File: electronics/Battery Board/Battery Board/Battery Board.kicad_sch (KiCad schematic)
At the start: 1 part

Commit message: Battery Protection Circuit
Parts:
- removed U?: MAX1924XEEE+, SOP63P602X175-16N, symbol MAX1924XEEE_:MAX1924XEEE+
- added BT1: BK-18650-PC8, BAT_BK-18650-PC8, symbol BK-18650-PC8:BK-18650-PC8
- added C1: 2.2uF, Capacitor_SMD:C_0805_2012Metric_Pad1.18x1.45mm_HandSolder, symbol Device:C_Small
- added C2, C4, C5, C6: 0.1uF, Capacitor_SMD:C_0805_2012Metric_Pad1.18x1.45mm_HandSolder, symbol Device:C_Small
- added C3: 1uF, Capacitor_SMD:C_0805_2012Metric_Pad1.18x1.45mm_HandSolder, symbol Device:C_Small
- added D1: D_Schottky, Bluesat:SOT91P240X102-3N, symbol Device:D_Schottky
- added Q1, Q2: IRF7404, Package_SO:SOIC-8_3.9x4.9mm_P1.27mm, symbol Transistor_FET:IRF7404
- added R1, R2, R3: 1K, Resistor_SMD:R_0603_1608Metric_Pad0.98x0.95mm_HandSolder, symbol Device:R
- added R4: 51, Resistor_SMD:R_0603_1608Metric_Pad0.98x0.95mm_HandSolder, symbol Device:R
- added R5, R6, R7: 10K, Resistor_SMD:R_0603_1608Metric_Pad0.98x0.95mm_HandSolder, symbol Device:R
- added R8: Rocket_Board, Bluesat:Rocket_Layout, symbol BlueSat:Rocket_Board
- added R_{SENSE}1: 0.02, Resistor_SMD:R_0603_1608Metric_Pad0.98x0.95mm_HandSolder, symbol Device:R
- added U1: MAX1924XEEE+, SOP63P602X175-16N, symbol MAX1924XEEE_:MAX1924XEEE+
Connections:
- new net: C2.1, D1.1 (K), U1.2 (VCC)
- new net: R1.1, U1.7 (B1P)
- new net: BT1.1+, BT1.2-, C5.1, C6.2, R1.2
- new net: R8.1 (5V), R8.18 (5V), R8.23 (5V), R8.33 (5V), R8.40 (5V), R8.8 (5V)
- new net: R8.10 (3.3V), R8.20 (3.3V), R8.21 (3.3V), R8.3 (3.3V), R8.31 (3.3V), R8.38 (3.3V)
- new net: R8.11 (GND), R8.14 (GND), R8.17 (GND), R8.19 (GND), R8.2 (GND), R8.22 (GND), R8.24 (GND), R8.27 (GND), R8.30 (GND), R8.32 (GND), R8.34 (GND), R8.37 (GND), R8.39 (GND), R8.4 (GND), R8.7 (GND), R8.9 (GND)
- new net: R3.1, U1.3 (B3P)
- new net: BT1.3+, BT1.4-, C3.1, C4.2, R3.2
- new net: R6.1, U1.12 (SHDN)
- new net: BT1.4+, C3.2, D1.2 (A), Q2.5 (D), Q2.6 (D), Q2.7 (D), Q2.8 (D), R4.2
- new net: R5.2, U1.11 (CTL)
- new net: C1.2, R7.1, U1.16 (SRC)
- new net: R4.1, U1.1 (B4P)
- new net: BT1.2+, BT1.3-, C4.1, C5.2, R2.2
- new net: Q1.1 (S), Q1.2 (S), Q1.3 (S), Q2.1 (S), Q2.2 (S), Q2.3 (S), R7.2
- new net: Q1.4 (G), U1.15 (~{DSO})
- new net: R2.1, U1.5 (B2P)
- new net: Q2.4 (G), U1.13 (~{TKO})
- new net GND: R_{SENSE}1.1, U1.10 (PKN)
- new net GNDPWR: BT1.1-, C1.1, C2.2, C6.1, R5.1, R6.2, R_{SENSE}1.2, U1.9 (BN)
- new net VPP: Q1.5 (D), Q1.6 (D), Q1.7 (D), Q1.8 (D)

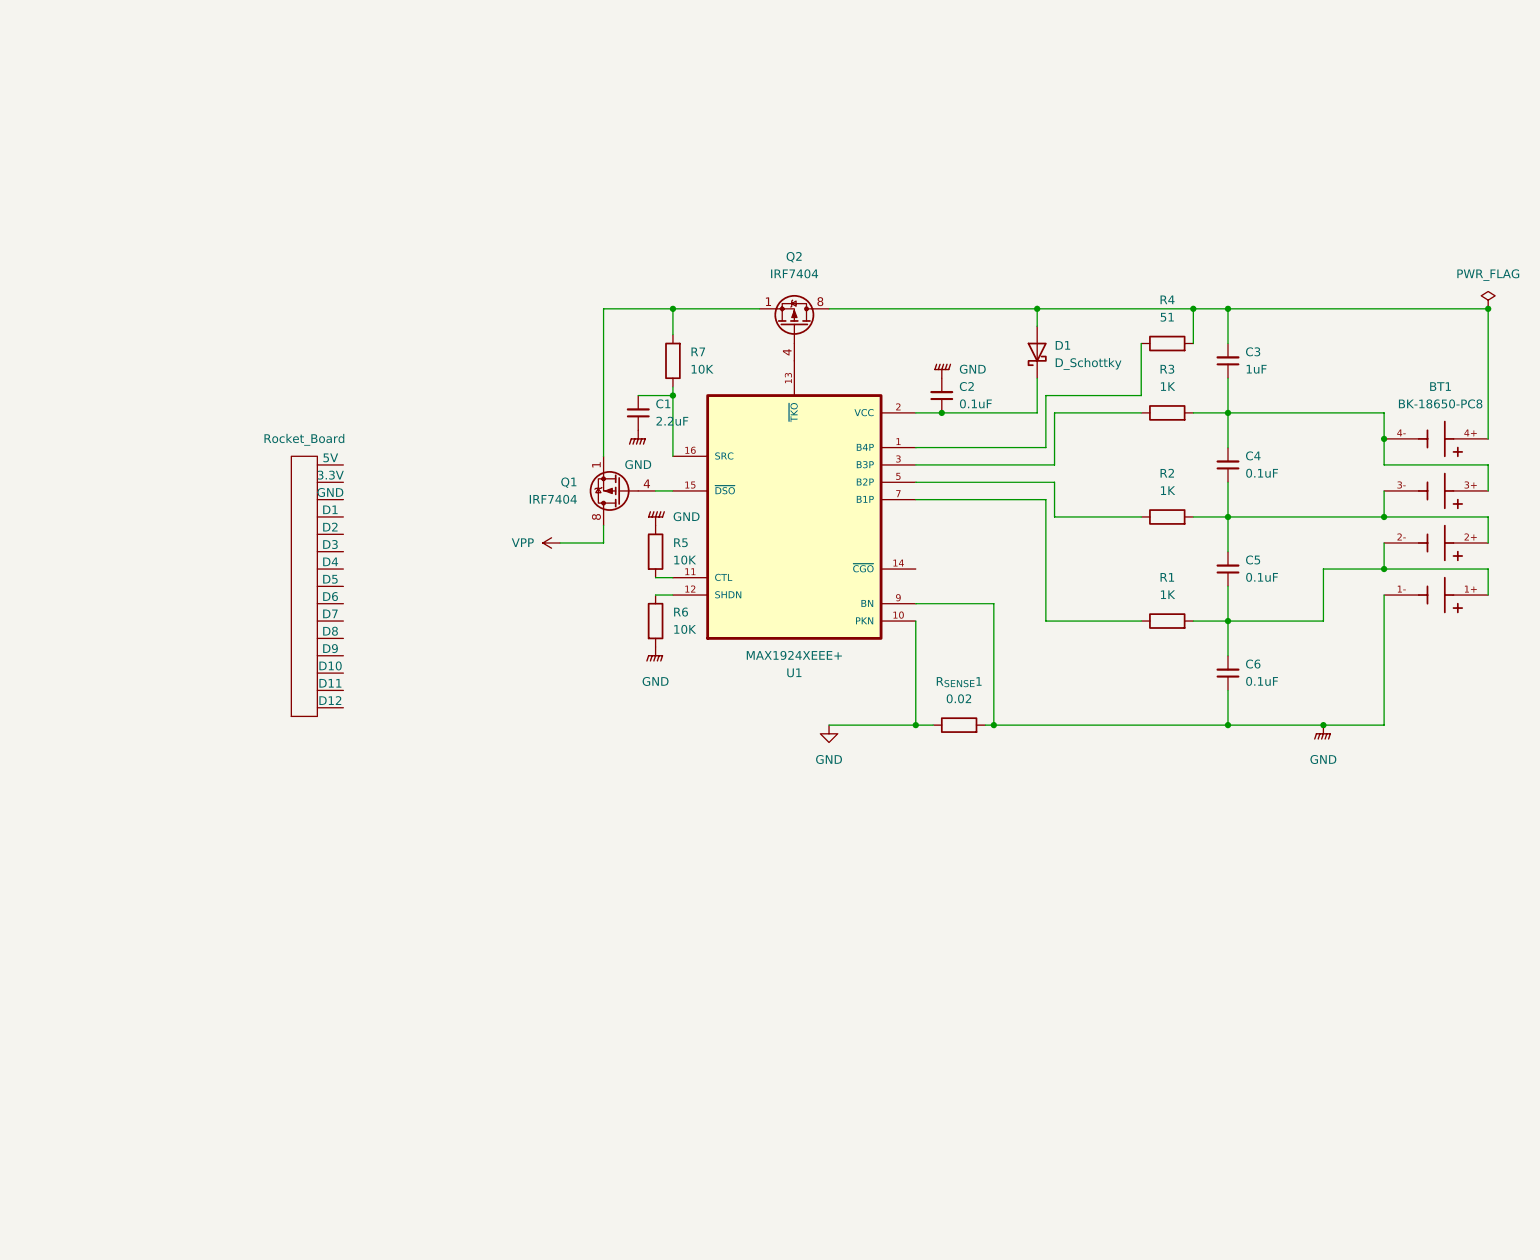
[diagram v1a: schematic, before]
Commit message: Batter Board almost finished
TODO
- Change mosfets&shunt resistor to new choice
- Adjust inductor for higher voltage
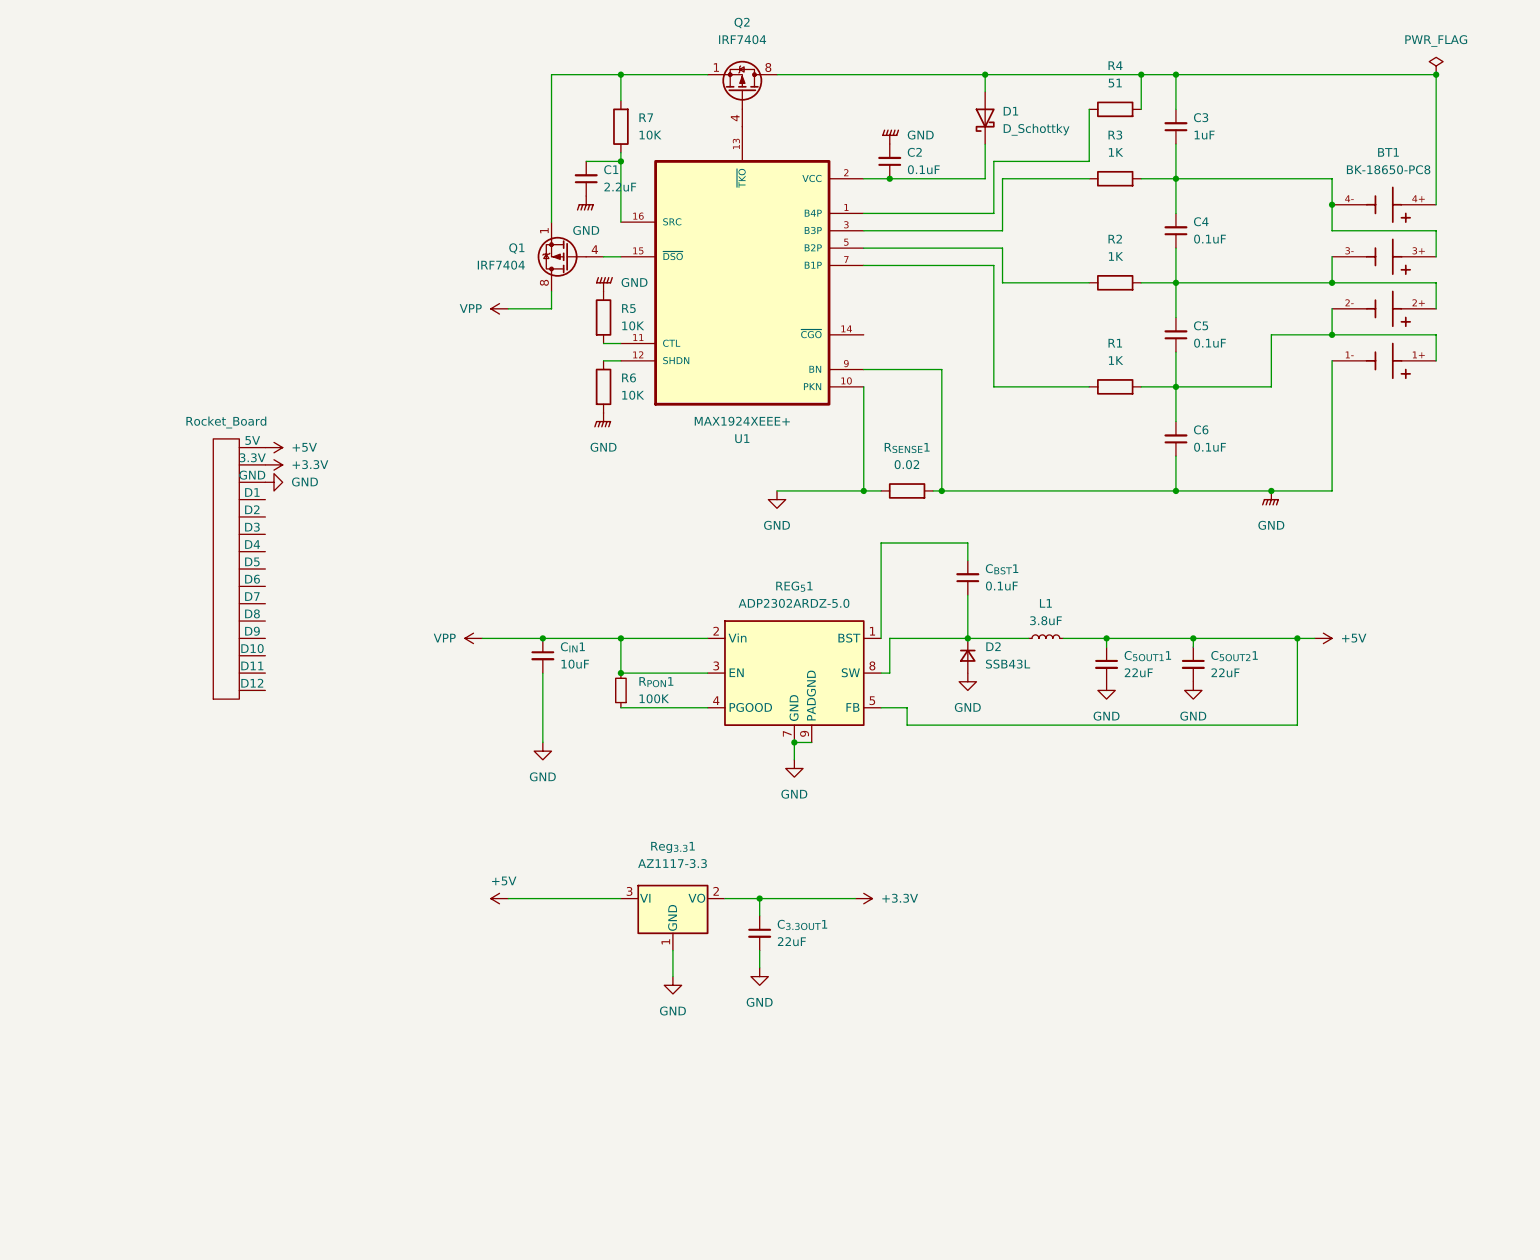
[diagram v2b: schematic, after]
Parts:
- added C_{3.3OUT}1, C_{5OUT1}1, C_{5OUT2}1: 22uF, Capacitor_SMD:C_0603_1608Metric_Pad1.08x0.95mm_HandSolder, symbol Device:C_Small
- added C_{BST}1: 0.1uF, Capacitor_SMD:C_0603_1608Metric_Pad1.08x0.95mm_HandSolder, symbol Device:C_Small
- added C_{IN}1: 10uF, Capacitor_SMD:C_0603_1608Metric_Pad1.08x0.95mm_HandSolder, symbol Device:C_Small
- added D2: SSB43L, Custom footprints:SSB43L hand solder, symbol Device:D_Small
- added L1: 3.8uF, Custom footprints:CDRH104R inductor, symbol Device:L_Small
- added REG_{5}1: ADP2302ARDZ-5.0, Package_SO:SOIC-8-1EP_3.9x4.9mm_P1.27mm_EP2.29x3mm, symbol Regulator_Switching:ADP2302ARDZ-5.0
- added R_{PON}1: 100K, Resistor_SMD:R_0603_1608Metric_Pad0.98x0.95mm_HandSolder, symbol Device:R_Small
- added Reg_{3.3}1: AZ1117-3.3, Package_TO_SOT_SMD:TO-252-2, symbol Regulator_Linear:AZ1117-3.3
- BT1: footprint BAT_BK-18650-PC8 -> Bluesat:BAT_BK-18650-PC8
- U1: footprint SOP63P602X175-16N -> Bluesat:SOP63P602X175-16N
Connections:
- net GND: now also R8.11 (GND), R8.14 (GND), R8.17 (GND), R8.19 (GND), R8.2 (GND), R8.22 (GND), R8.24 (GND), R8.27 (GND), R8.30 (GND), R8.32 (GND), R8.34 (GND), R8.37 (GND), R8.39 (GND), R8.4 (GND), R8.7 (GND), R8.9 (GND), C_{3.3OUT}1.2, C_{5OUT1}1.2, C_{5OUT2}1.2, C_{IN}1.2, D2.2 (A), REG_{5}1.7 (GND), REG_{5}1.9 (PADGND), Reg_{3.3}1.1 (GND)
- net VPP: now also C_{IN}1.1, REG_{5}1.2 (Vin), REG_{5}1.3 (EN), R_{PON}1.2
- net +5V: now reaches R8.1 (5V), R8.18 (5V), R8.23 (5V), R8.33 (5V), R8.40 (5V), R8.8 (5V)
- net +5V: now also C_{5OUT1}1.1, C_{5OUT2}1.1, L1.2, REG_{5}1.5 (FB), Reg_{3.3}1.3 (VI)
- net +3V3: now reaches R8.10 (3.3V), R8.20 (3.3V), R8.21 (3.3V), R8.3 (3.3V), R8.31 (3.3V), R8.38 (3.3V)
- net +3V3: now also C_{3.3OUT}1.1, Reg_{3.3}1.2 (VO)
- new net: C_{BST}1.1, D2.1 (K), L1.1, REG_{5}1.8 (SW)
- new net: C_{BST}1.2, REG_{5}1.1 (BST)
- new net: REG_{5}1.4 (PGOOD), R_{PON}1.1
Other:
- moved on the sheet: BT1, C1, C2, C3, C4, C5, C6, D1, Q1, Q2, R1, R2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

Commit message: Finalised PCB, working schematic
Sending to Fab tomorrow, schematic could do with a little cleanup.
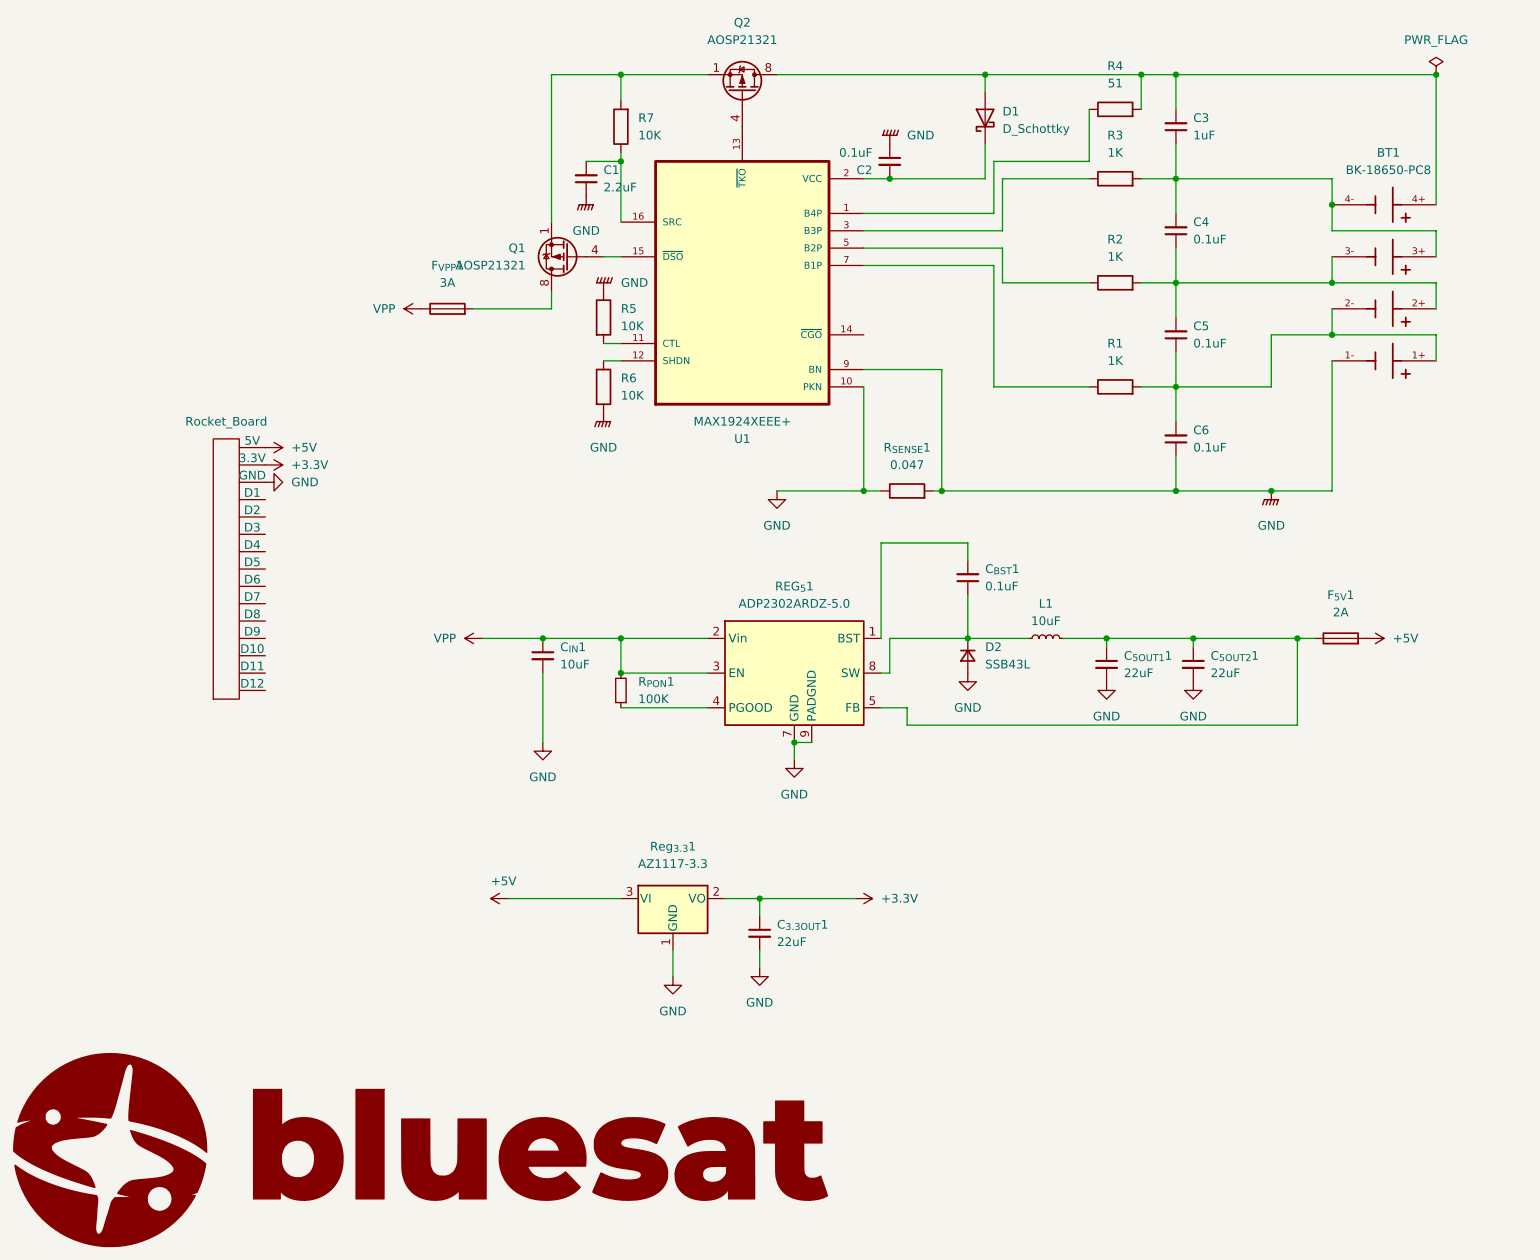
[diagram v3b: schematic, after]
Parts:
- added F_{5V}1: 2A, Fuse:Fuse_1206_3216Metric_Pad1.42x1.75mm_HandSolder, symbol Device:Fuse
- added F_{VPP}1: 3A, Fuse:Fuse_1206_3216Metric_Pad1.42x1.75mm_HandSolder, symbol Device:Fuse
- L1: value 3.8uF -> 10uF
- Q1, Q2: value IRF7404 -> AOSP21321
- R_{SENSE}1: value 0.02 -> 0.047; footprint Resistor_SMD:R_0603_1608Metric_Pad0.98x0.95mm_HandSolder -> Bluesat:WSHP2818 Shunt resistor Vishay
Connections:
- net +5V: now also F_{5V}1.2; no longer C_{5OUT1}1.1, C_{5OUT2}1.1, L1.2, REG_{5}1.5 (FB)
- net GNDPWR: now also C2.1; no longer C2.2
- net VPP: now also F_{VPP}1.1; no longer Q1.5 (D), Q1.6 (D), Q1.7 (D), Q1.8 (D)
- net at D1.1 (K), U1.2 (VCC): now also C2.2; no longer C2.1
- new net: C_{5OUT1}1.1, C_{5OUT2}1.1, F_{5V}1.1, L1.2, REG_{5}1.5 (FB)
- new net: F_{VPP}1.2, Q1.5 (D), Q1.6 (D), Q1.7 (D), Q1.8 (D)
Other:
- moved on the sheet: C2
